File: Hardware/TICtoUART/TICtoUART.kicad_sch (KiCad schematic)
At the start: 11 parts, among them J3 Conn_01x02_Male

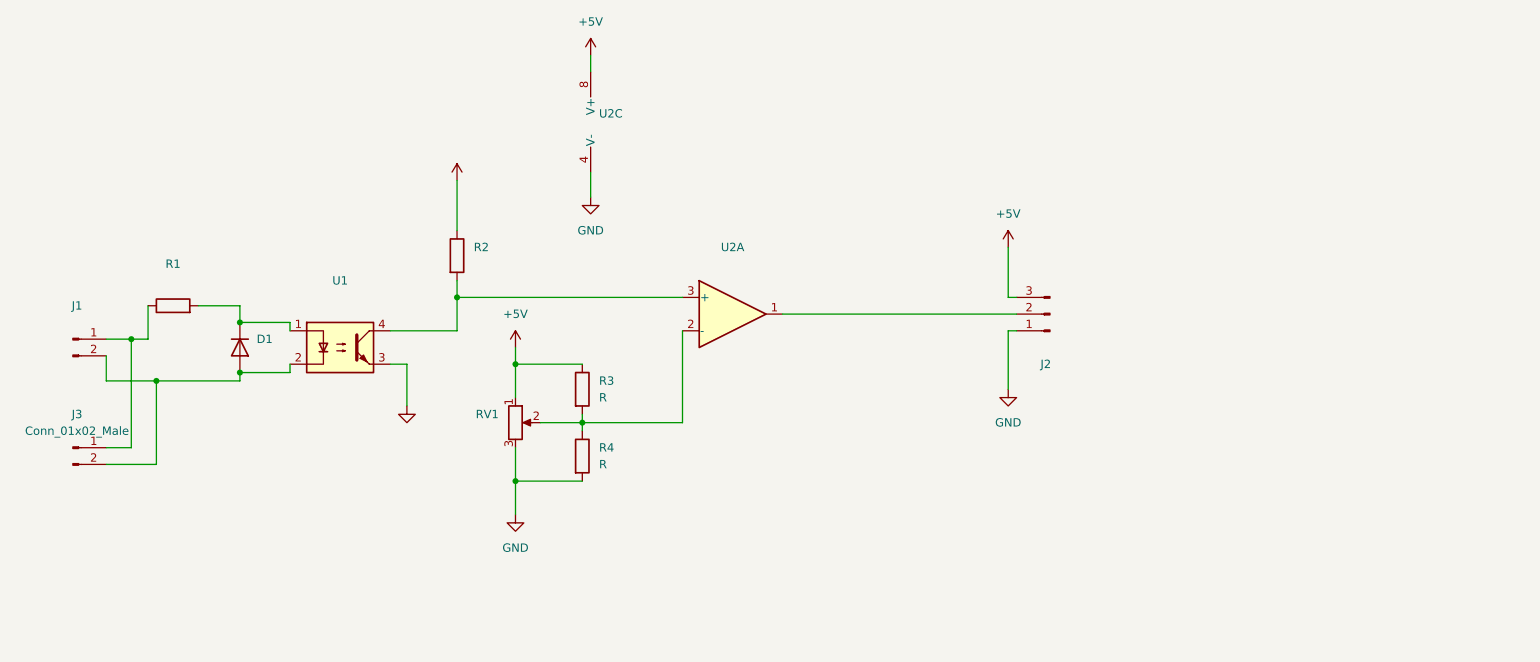
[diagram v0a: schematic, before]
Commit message: added MQTT + status LED
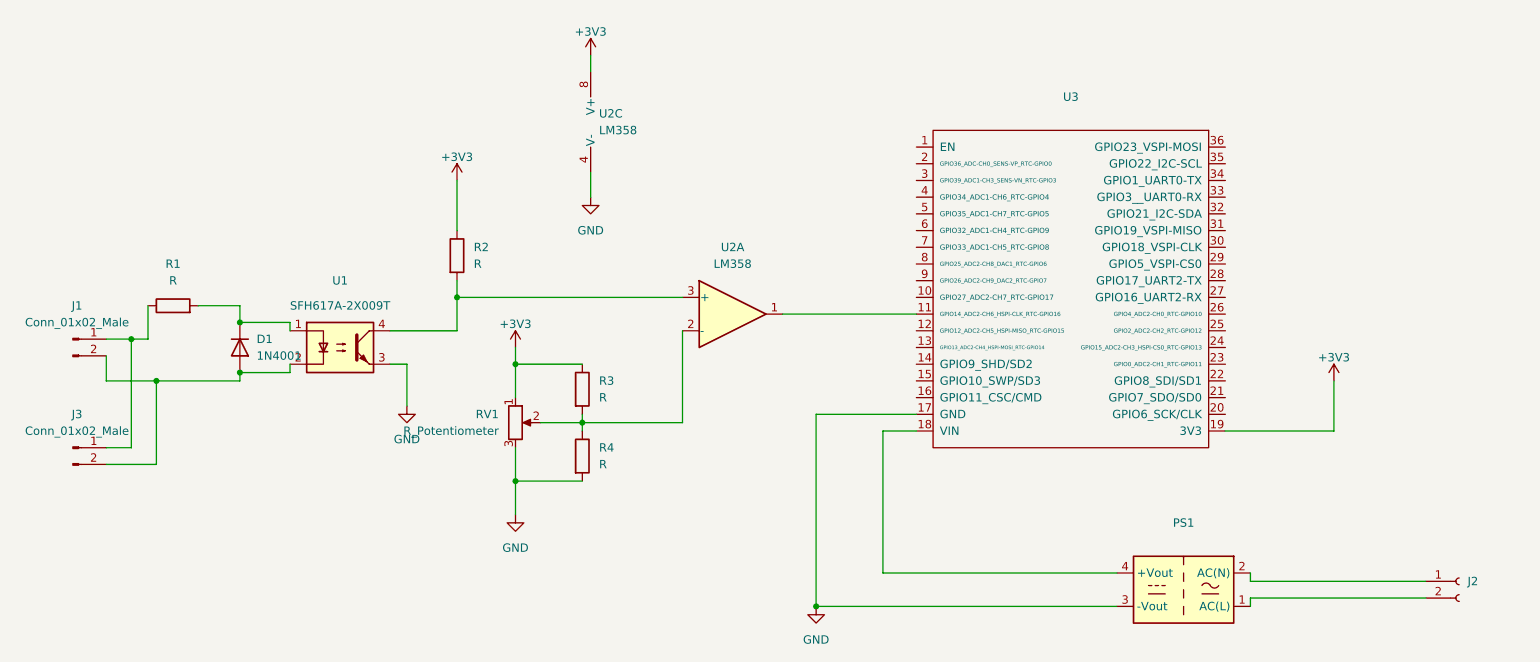
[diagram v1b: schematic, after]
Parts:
- removed J2: (no value), symbol Connector:Conn_01x03_Male
- added J2: (no value), symbol Connector:Conn_01x02_Female
- added PS1: (no value), symbol Converter_ACDC:RAC01-05SGB
- added U3: (no value), symbol doit-esp32-devkit-v1:DOIT-ESP32-DEVKIT-V1
- D1: value (none) -> 1N4001; footprint (none) -> Diode_THT:D_DO-41_SOD81_P10.16mm_Horizontal
- J1: value (none) -> Conn_01x02_Male; footprint (none) -> Connector_PinHeader_2.54mm:PinHeader_1x02_P2.54mm_Vertical
- J3: footprint (none) -> Connector_Wire:SolderWire-1sqmm_1x02_P7.8mm_D1.4mm_OD3.9mm
- R1, R2: value (none) -> R; footprint (none) -> Resistor_THT:R_Axial_DIN0207_L6.3mm_D2.5mm_P10.16mm_Horizontal
- R3, R4: footprint (none) -> Resistor_SMD:R_0805_2012Metric_Pad1.20x1.40mm_HandSolder
- RV1: value (none) -> R_Potentiometer; footprint (none) -> Potentiometer_THT:Potentiometer_Bourns_3266Y_Vertical
- U1: value (none) -> SFH617A-2X009T; footprint (none) -> Package_DIP:DIP-4_W7.62mm_Socket
- U2: value (none) -> LM358; footprint (none) -> Package_DIP:DIP-8_W7.62mm_Socket_LongPads
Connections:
- net GND: now also PS1.3 (-Vout), U3.17 (GND)
- net at U2.1: now also U3.11 (GPIO14_ADC2-CH6_HSPI-CLK_RTC-GPIO16)
- net +5V renamed +3V3
- net +3V3: now also U3.19 (3V3)
- new net: J2.1 (Pin_1), PS1.2 (AC(N))
- new net: J2.2 (Pin_2), PS1.1 (AC(L))
- new net: PS1.4 (+Vout), U3.18 (VIN)

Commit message: Fully reworked PCB to host an ESP32 devkit Added CAD for enclosuer
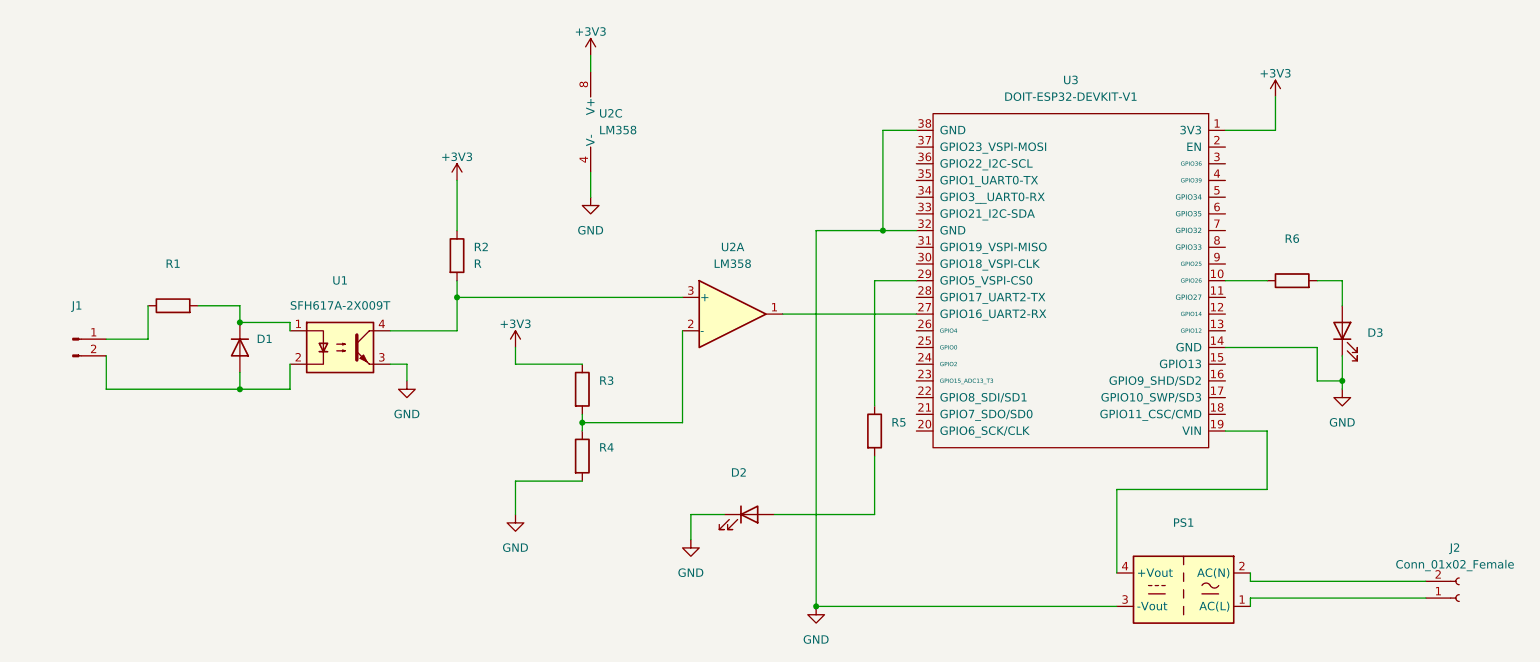
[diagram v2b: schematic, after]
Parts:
- removed J3: Conn_01x02_Male, Connector_Wire:SolderWire-1sqmm_1x02_P7.8mm_D1.4mm_OD3.9mm, symbol Connector:Conn_01x02_Male
- removed RV1: R_Potentiometer, Potentiometer_THT:Potentiometer_Bourns_3266Y_Vertical, symbol Device:R_Potentiometer
- added D2, D3: (no value), symbol Device:LED
- added R5, R6: (no value), symbol Device:R
- D1: value 1N4001 -> (none); footprint Diode_THT:D_DO-41_SOD81_P10.16mm_Horizontal -> (none)
- J1: value Conn_01x02_Male -> (none); footprint Connector_PinHeader_2.54mm:PinHeader_1x02_P2.54mm_Vertical -> (none)
- J2: value (none) -> Conn_01x02_Female; footprint (none) -> Connector_Phoenix_MSTB:PhoenixContact_MSTBA_2,5_2-G_1x02_P5.00mm_Horizontal
- R1: value R -> (none); footprint Resistor_THT:R_Axial_DIN0207_L6.3mm_D2.5mm_P10.16mm_Horizontal -> (none)
- R3, R4: value R -> (none); footprint Resistor_SMD:R_0805_2012Metric_Pad1.20x1.40mm_HandSolder -> (none)
- U3: value (none) -> DOIT-ESP32-DEVKIT-V1; footprint (none) -> doit-esp32-devkit-kicad-master:ESP_WROOM_32-DOIT-DEVKIT; symbol doit-esp32-devkit-v1:DOIT-ESP32-DEVKIT-V1 -> doit-esp32-devkit-v1:DOIT-ESP_WROOM_32-DEVKIT-V1
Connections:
- net +3V3: now also U3.1 (3V3); no longer U3.19 (3V3)
- net GND: now also U3.14 (GND), U3.32 (GND), U3.38 (GND), D2.1 (K), D3.1 (K); no longer U3.17 (GND)
- net at U2.1: now also U3.27 (GPIO16_UART2-RX); no longer U3.11 (GPIO14_ADC2-CH6_HSPI-CLK_RTC-GPIO16)
- net at J2.1 (Pin_1): now also PS1.1 (AC(L)); no longer PS1.2 (AC(N))
- net at J2.2 (Pin_2): now also PS1.2 (AC(N)); no longer PS1.1 (AC(L))
- net at U3.10 (GPIO26): now also R6.1
- net at U3.18 (GPIO11_CSC/CMD): no longer PS1.4 (+Vout)
- net at U3.29 (GPIO5_VSPI-CS0): now also R5.1
- new net: D2.2 (A), R5.2
- new net: D3.2 (A), R6.2
- new net: PS1.4 (+Vout), U3.19 (VIN)
